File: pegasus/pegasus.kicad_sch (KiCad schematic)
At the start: 11 parts, among them IC1 Adafruit_MPL3115A2, IC2 Adafruit-BNO055-PCB, IC3 L70B-M39, IC4 RFD900, IC5 L7805ACV, J1 Conn_01x02_Female, J2 Conn_01x02_Female, J3 Conn_01x02_Female, J4 Conn_Coaxial, J5 Conn_Coaxial, U1 Teensy4.1

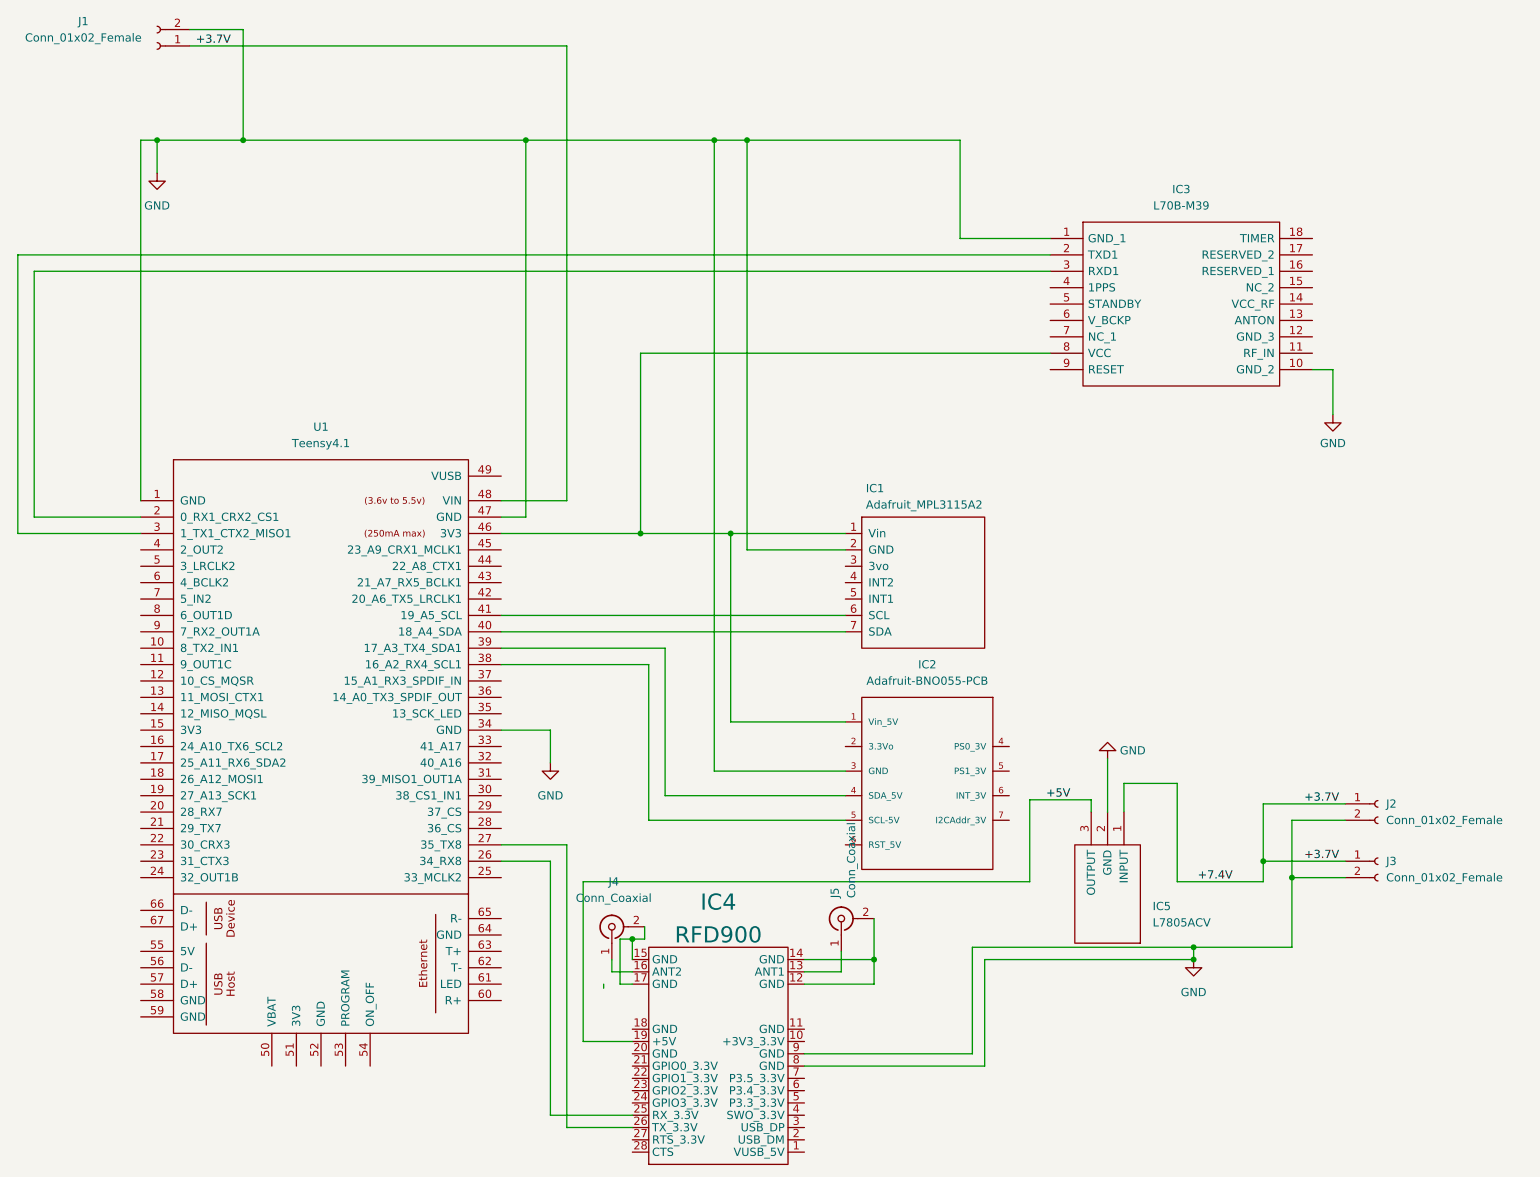
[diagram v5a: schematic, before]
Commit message: removed one of connectors, fixed connector schematic wiring
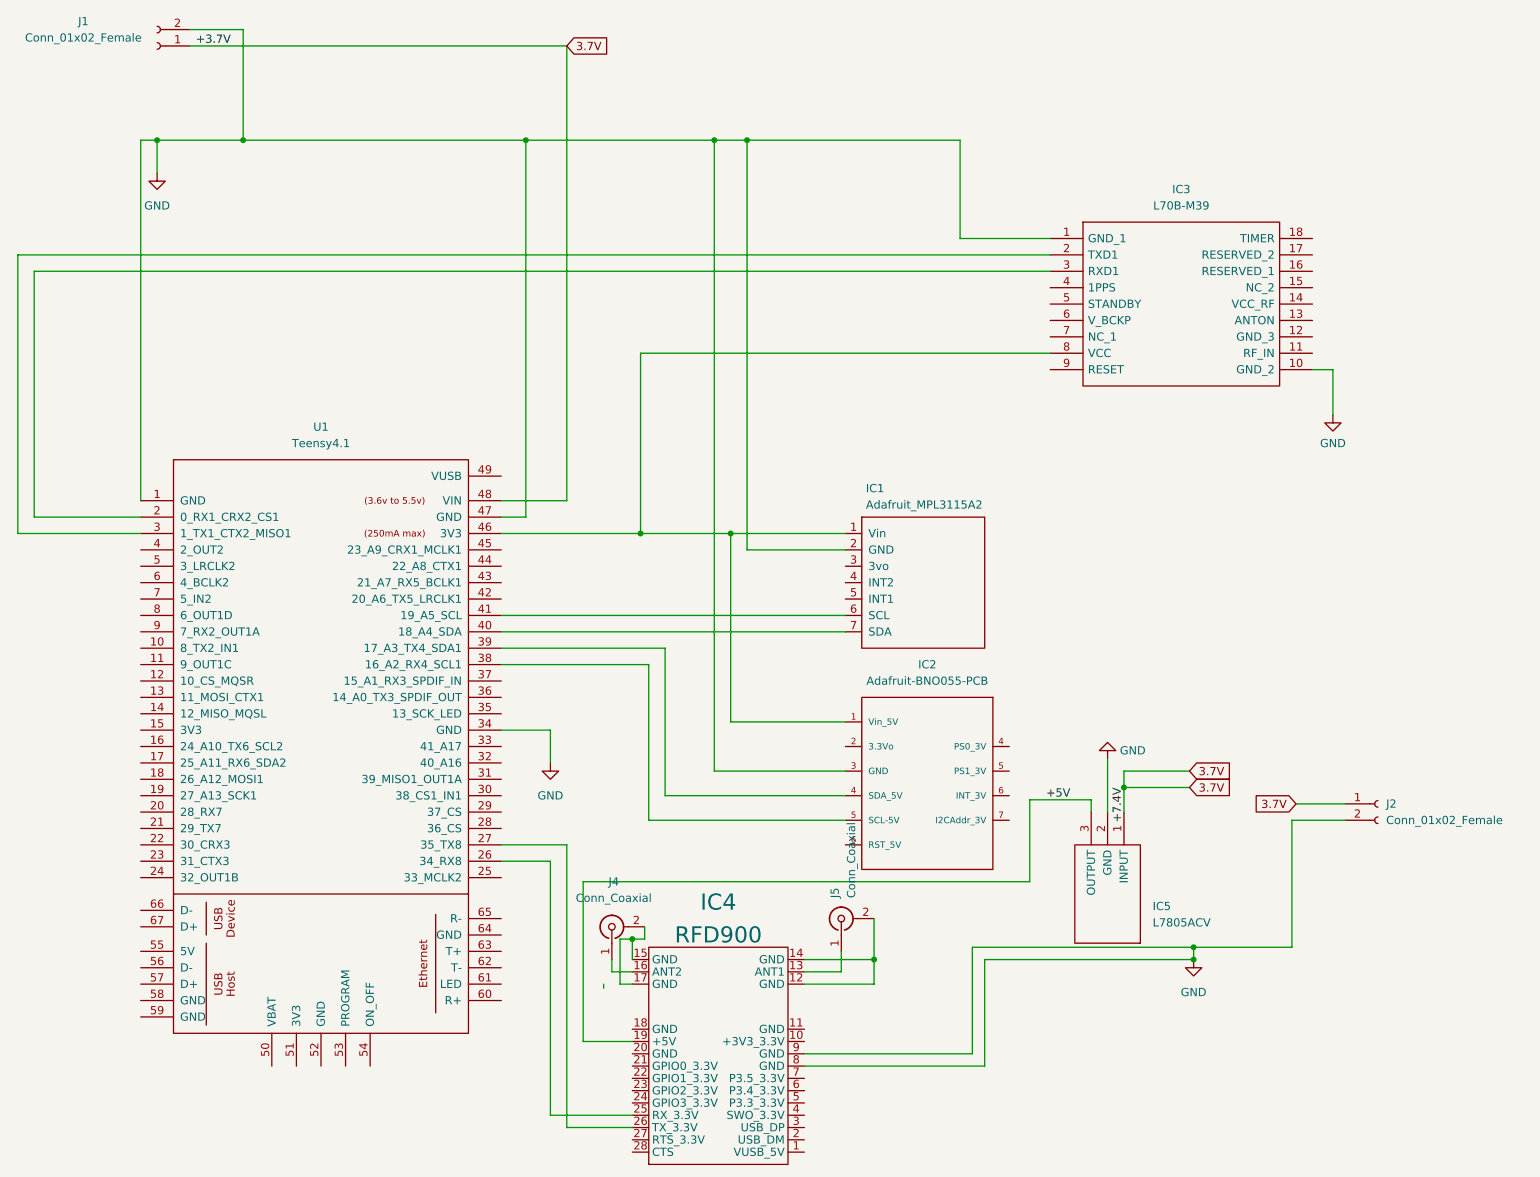
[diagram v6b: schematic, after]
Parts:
- removed J3: Conn_01x02_Female, Connector_PinHeader_2.00mm:PinHeader_1x02_P2.00mm_Vertical, symbol Connector:Conn_01x02_Female
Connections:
- net +3.7V renamed 3.7V
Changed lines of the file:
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@@
   (junction (at 101.6 35.56) (diameter 0) (color 0 0 0 0)
   )
-  (junction (at 220.345 149.86) (diameter 0) (color 0 0 0 0)
-  )
   (junction (at 135.89 35.56) (diameter 0) (color 0 0 0 0)
   )
@@
   (junction (at 130.81 35.56) (diameter 0) (color 0 0 0 0)
   )
+  (junction (at 194.31 135.89) (diameter 0) (color 0 0 0 0)
+  )
   (junction (at 133.35 96.52) (diameter 0) (color 0 0 0 0)
   )
   (junction (at 44.45 35.56) (diameter 0) (color 0 0 0 0)
   )
-  (junction (at 215.9 147.32) (diameter 0) (color 0 0 0 0)
-  )
   (junction (at 119.38 96.52) (diameter 0) (color 0 0 0 0)
   )
@@
     (stroke (width 0) (type default) (color 0 0 0 0))
   )
+  (wire (pts (xy 194.31 139.7) (xy 194.31 135.89))
+    (stroke (width 0) (type default) (color 0 0 0 0))
+  )
   (wire (pts (xy 144.78 164.465) (xy 150.495 164.465))
     (stroke (width 0) (type default) (color 0 0 0 0))
   )
-  (wire (pts (xy 220.345 149.86) (xy 228.6 149.86))
-    (stroke (width 0) (type default) (color 0 0 0 0))
-  )
   (wire (pts (xy 223.52 71.12) (xy 226.695 71.12))
     (stroke (width 0) (type default) (color 0 0 0 0))
@@
     (stroke (width 0) (type default) (color 0 0 0 0))
   )
+  (wire (pts (xy 194.31 133.35) (xy 204.47 133.35))
+    (stroke (width 0) (type default) (color 0 0 0 0))
+  )
   (wire (pts (xy 205.105 160.655) (xy 205.105 162.56))
     (stroke (width 0) (type default) (color 0 0 0 0))
@@
     (stroke (width 0) (type default) (color 0 0 0 0))
   )
-  (wire (pts (xy 228.6 147.32) (xy 215.9 147.32))
-    (stroke (width 0) (type default) (color 0 0 0 0))
-  )
   (wire (pts (xy 105.41 186.69) (xy 105.41 147.32))
     (stroke (width 0) (type default) (color 0 0 0 0))
@@
     (stroke (width 0) (type default) (color 0 0 0 0))
   )
-  (wire (pts (xy 220.345 149.86) (xy 220.345 160.655))
+  (wire (pts (xy 220.345 140.97) (xy 220.345 160.655))
     (stroke (width 0) (type default) (color 0 0 0 0))
   )
@@
     (stroke (width 0) (type default) (color 0 0 0 0))
   )
-  (wire (pts (xy 215.9 138.43) (xy 228.6 138.43))
-    (stroke (width 0) (type default) (color 0 0 0 0))
-  )
   (wire (pts (xy 97.79 96.52) (xy 119.38 96.52))
     (stroke (width 0) (type default) (color 0 0 0 0))
@@
     (stroke (width 0) (type default) (color 0 0 0 0))
   )
-  (wire (pts (xy 220.345 140.97) (xy 220.345 149.86))
-    (stroke (width 0) (type default) (color 0 0 0 0))
-  )
   (wire (pts (xy 97.79 93.98) (xy 101.6 93.98))
     (stroke (width 0) (type default) (color 0 0 0 0))
@@
     (stroke (width 0) (type default) (color 0 0 0 0))
   )
-  (wire (pts (xy 215.9 147.32) (xy 215.9 138.43))
-    (stroke (width 0) (type default) (color 0 0 0 0))
-  )
   (wire (pts (xy 144.78 177.165) (xy 170.815 177.165))
     (stroke (width 0) (type default) (color 0 0 0 0))
@@
     (stroke (width 0) (type default) (color 0 0 0 0))
   )
-  (wire (pts (xy 202.565 135.255) (xy 194.31 135.255))
-    (stroke (width 0) (type default) (color 0 0 0 0))
-  )
-  (wire (pts (xy 194.31 135.255) (xy 194.31 139.7))
-    (stroke (width 0) (type default) (color 0 0 0 0))
-  )
   (wire (pts (xy 170.815 160.655) (xy 205.105 160.655))
     (stroke (width 0) (type default) (color 0 0 0 0))
   )
+  (wire (pts (xy 220.98 138.43) (xy 228.6 138.43))
+    (stroke (width 0) (type default) (color 0 0 0 0))
+  )
   (wire (pts (xy 155.575 162.56) (xy 155.575 156.21))
     (stroke (width 0) (type default) (color 0 0 0 0))
   )
-  (wire (pts (xy 202.565 150.495) (xy 215.9 150.495))
-    (stroke (width 0) (type default) (color 0 0 0 0))
-  )
   (wire (pts (xy 97.79 114.3) (xy 123.19 114.3))
     (stroke (width 0) (type default) (color 0 0 0 0))
@@
     (stroke (width 0) (type default) (color 0 0 0 0))
   )
-  (wire (pts (xy 215.9 150.495) (xy 215.9 147.32))
-    (stroke (width 0) (type default) (color 0 0 0 0))
-  )
   (wire (pts (xy 191.77 131.445) (xy 191.77 139.7))
     (stroke (width 0) (type default) (color 0 0 0 0))
   )
+  (wire (pts (xy 194.31 135.89) (xy 204.47 135.89))
+    (stroke (width 0) (type default) (color 0 0 0 0))
+  )
   (wire (pts (xy 22.86 53.34) (xy 182.88 53.34))
     (stroke (width 0) (type default) (color 0 0 0 0))
@@
     (stroke (width 0) (type default) (color 0 0 0 0))
   )
+  (wire (pts (xy 194.31 135.89) (xy 194.31 133.35))
+    (stroke (width 0) (type default) (color 0 0 0 0))
+  )
   (wire (pts (xy 116.205 166.37) (xy 116.205 159.385))
     (stroke (width 0) (type default) (color 0 0 0 0))
@@
     (stroke (width 0) (type default) (color 0 0 0 0))
   )
-  (wire (pts (xy 202.565 150.495) (xy 202.565 135.255))
-    (stroke (width 0) (type default) (color 0 0 0 0))
-  )
   (wire (pts (xy 114.935 164.465) (xy 118.11 164.465))
     (stroke (width 0) (type default) (color 0 0 0 0))
@@
   (wire (pts (xy 97.79 109.22) (xy 151.13 109.22))
     (stroke (width 0) (type default) (color 0 0 0 0))
-  )
-  (label "+7.4V" (at 205.74 150.495 0)
-    (effects (font (size 1.27 1.27)) (justify left bottom))
   )
   (label "+3.7V" (at 55.88 20.955 180)
     (effects (font (size 1.27 1.27)) (justify right bottom))
   )
-  (label "+3.7V" (at 222.25 147.32 0)
-    (effects (font (size 1.27 1.27)) (justify left bottom))
-  )
-  (label "+3.7V" (at 222.25 138.43 0)
-    (effects (font (size 1.27 1.27)) (justify left bottom))
-  )
   (label "+5V" (at 182.245 137.795 0)
     (effects (font (size 1.27 1.27)) (justify left bottom))
+  )
+  (label "+7.4V" (at 194.31 135.89 270)
+    (effects (font (size 1.27 1.27)) (justify right bottom))
+  )
+  (global_label "3.7V" (shape input) (at 220.98 138.43 180) (fields_autoplaced)
+    (effects (font (size 1.27 1.27)) (justify right))
+    (property "Intersheet References" "${INTERSHEET_REFS}" (id 0) (at 214.4545 138.3506 0)
+      (effects (font (size 1.27 1.27)) (justify right) hide)
+    )
+  )
+  (global_label "3.7V" (shape input) (at 107.95 20.955 0) (fields_autoplaced)
+    (effects (font (size 1.27 1.27)) (justify left))
+    (property "Intersheet References" "${INTERSHEET_REFS}" (id 0) (at 114.4755 20.8756 0)
+      (effects (font (size 1.27 1.27)) (justify left) hide)
+    )
+  )
+  (global_label "3.7V" (shape input) (at 204.47 135.89 0) (fields_autoplaced)
+    (effects (font (size 1.27 1.27)) (justify left))
+    (property "Intersheet References" "${INTERSHEET_REFS}" (id 0) (at 210.9955 135.8106 0)
+      (effects (font (size 1.27 1.27)) (justify left) hide)
+    )
+  )
+  (global_label "3.7V" (shape input) (at 204.47 133.35 0) (fields_autoplaced)
+    (effects (font (size 1.27 1.27)) (justify left))
+    (property "Intersheet References" "${INTERSHEET_REFS}" (id 0) (at 210.9955 133.2706 0)
+      (effects (font (size 1.27 1.27)) (justify left) hide)
+    )
   )
   (symbol (lib_id "power:GND") (at 105.41 132.08 0) (unit 1)
@@
     (pin "2")
   )
-  (symbol (lib_id "Connector:Conn_01x02_Female") (at 233.68 147.32 0) (unit 1)
-    (in_bom yes) (on_board yes) (fields_autoplaced)
-    (property "Reference" "J3" (id 0) (at 234.95 147.3199 0)
-      (effects (font (size 1.27 1.27)) (justify left))
-    )
-    (property "Value" "Conn_01x02_Female" (id 1) (at 234.95 149.8599 0)
-      (effects (font (size 1.27 1.27)) (justify left))
-    )
-    (property "Footprint" "Connector_PinHeader_2.00mm:PinHeader_1x02_P2.00mm_Vertical" (id 2) (at 233.68 147.32 0)
-      (effects (font (size 1.27 1.27)) hide)
-    )
-    (property "Datasheet" "~" (id 3) (at 233.68 147.32 0)
-      (effects (font (size 1.27 1.27)) hide)
-    )
-    (pin "1")
-    (pin "2")
-  )
   (symbol (lib_id "power:GND") (at 226.695 78.105 0) (unit 1)
     (in_bom yes) (on_board yes) (fields_autoplaced)
@@
       (reference "J2") (unit 1) (value "Conn_01x02_Female") (footprint "Connector_PinHeader_2.00mm:PinHeader_1x02_P2.00mm_Vertical")
     )
-    (path "/419715bf-ffaa-4f14-ba39-b7cca3633324"
-      (reference "J3") (unit 1) (value "Conn_01x02_Female") (footprint "Connector_PinHeader_2.00mm:PinHeader_1x02_P2.00mm_Vertical")
-    )
     (path "/3ccf6afc-bd28-4aa2-895e-eba52cf09e27"

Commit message: created sma-connector schematic and footprint and implemented 3D step file
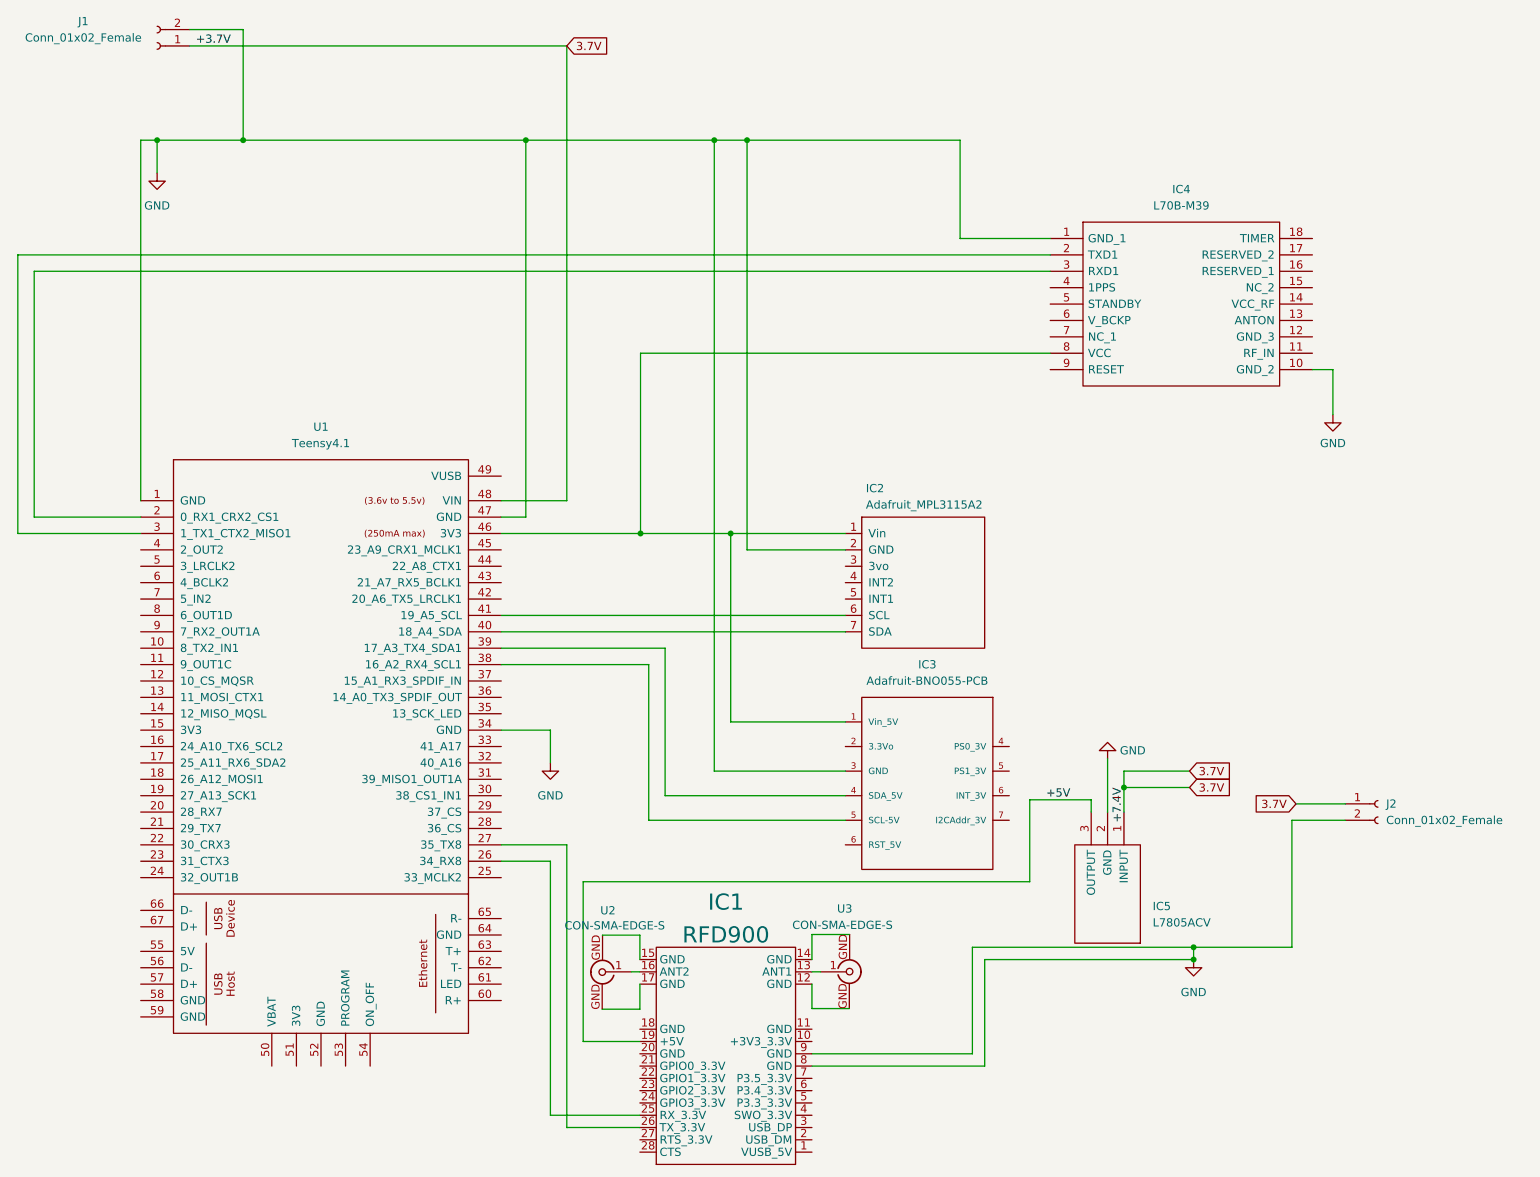
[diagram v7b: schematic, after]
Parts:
- removed J4, J5: Conn_Coaxial, Connector_Coaxial:SMA_Molex_73251-1153_EdgeMount_Horizontal, symbol Connector:Conn_Coaxial
- added U2, U3: CON-SMA-EDGE-S, SMA-Connectors:RFSOLUTIONS_CON-SMA-EDGE-S, symbol sma-connectors:CON-SMA-EDGE-S
- renumbered IC4 to IC1, IC1 to IC2, IC2 to IC3, IC3 to IC4
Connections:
- net at IC1.16 (ANT2): now also U2.1
- net at IC1.15 (GND): now also U2.GND; no longer IC1.17 (GND)
- net at IC1.13 (ANT1): now also U3.1
- net at IC1.12 (GND): now also U3.GND; no longer IC1.14 (GND)
- new net: IC1.17 (GND), U2.GND
- new net: IC1.14 (GND), U3.GND
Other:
- moved on the sheet: IC1
